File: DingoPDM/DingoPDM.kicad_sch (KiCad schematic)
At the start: 6 parts

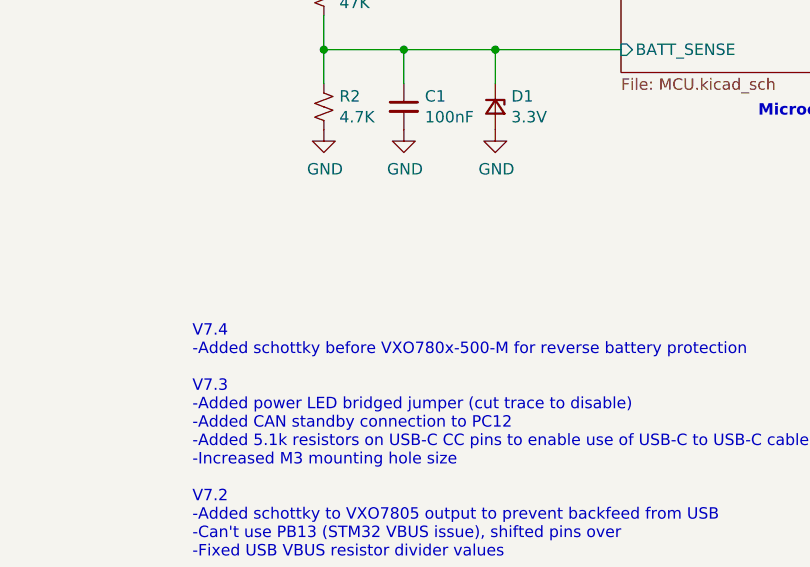
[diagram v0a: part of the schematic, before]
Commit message: add DC-DC converter options
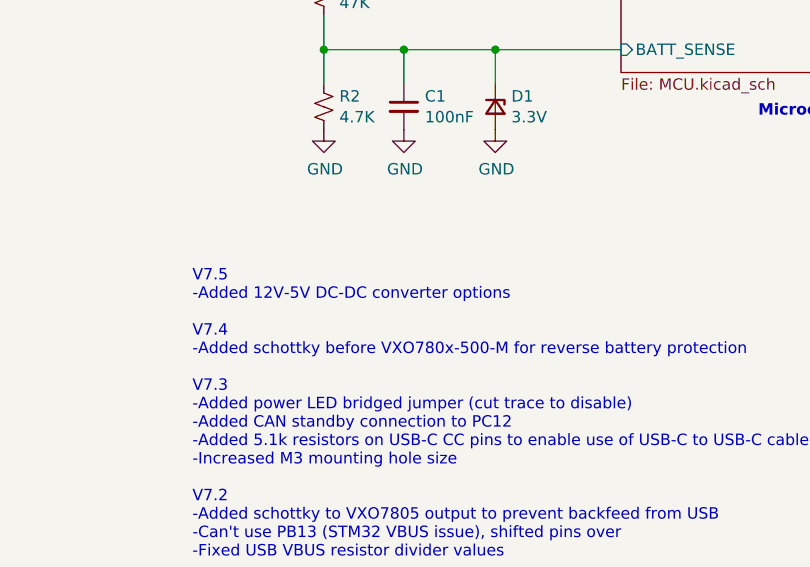
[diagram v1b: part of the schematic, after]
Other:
- note added: "V7.5 -Added 12V-5V DC-DC converter options V7.4 -Added schottky before VXO780x-500-M for reverse battery protection V7.3 -Added power LED bridged jumper (cut trace to disable) -Added CAN standby connection to PC12 -Added 5.1k resistors on USB-C CC pins to enable use of USB-C to USB-C cable -Increased M3 mounting hole size V7.2 -Added schottky to VXO7805 output to prevent backfeed from USB -Can't 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"
- note removed: "V7.4 -Added schottky before VXO780x-500-M for reverse battery protection V7.3 -Added power LED bridged jumper (cut trace to disable) -Added CAN standby connection to PC12 -Added 5.1k resistors on USB-C CC pins to enable use of USB-C to USB-C cable -Increased M3 mounting hole size V7.2 -Added schottky to VXO7805 output to prevent backfeed from USB -Can't use PB13 (STM32 VBUS issue), shifted pins o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"
- title: Dingo_PDM -> dingoPDM
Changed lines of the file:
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@@
 (kicad_sch
-	(version 20231120)
+	(version 20250114)
 	(generator "eeschema")
-	(generator_version "8.0")
+	(generator_version "9.0")
 	(paper "USLetter")
 	(title_block
-		(title "Dingo_PDM")
-		(date "2024-05-26")
-		(rev "v7.3")
+		(title "dingoPDM")
+		(date "2025-05-06")
+		(rev "v7.5")
 		(comment 3 "github.com/corygrant")
 		(comment 4 "Cory Grant")
+	)
+	(text "Microcontroller"
+		(exclude_from_sim no)
+		(at 132.715 120.65 0)
+		(effects
+			(font
+				(size 1.27 1.27)
+				(thickness 0.254)
+				(bold yes)
+			)
+			(justify left bottom)
+		)
+	)
+	(text "V7.5 \n-Added 12V-5V DC-DC converter options\n\nV7.4\n-Added schottky before VXO780x-500-M for reverse battery protection\n\nV7.3\n-Added power LED bridged jumper (cut trace to disable)\n-Added CAN standby connection to PC12\n-Added 5.1k resistors on USB-C CC pins to enable use of USB-C to USB-C cable\n-Increased M3 mounting hole size\n\nV7.2\n-Added schottky to VXO7805 output to prevent backfeed from USB\n-Can't use PB13 (STM32 VBUS issue), shifted pins over\n-Fixed USB VBUS resistor divider values\n\nV7.1\n-Fixed FRAM SCL/SDA backwards\n-Changed top copper fill from solid to thermal reliefs to make soldering easier\n-Added 2x status LEDs\n-Fixed silkscreen\n\nV7\n-Changed to STM32F446RET6\n-Added USB again, for DFU and easy settings change\n-Switched BTS724 to 2x BTS7008-2EPA\n-Added another op-amp for IS\n-Added boot selector again to enable DFU\n"
+		(exclude_from_sim no)
+		(at 69.85 196.215 0)
+		(effects
+			(font
+				(size 1.27 1.27)
+			)
+			(justify left bottom)
+		)
 	)
 	(junction
@@
 			(width 0)
 			(type default)
-		)
-	)
-	(text "Microcontroller"
-		(exclude_from_sim no)
-		(at 132.715 120.65 0)
-		(effects
-			(font
-				(size 1.27 1.27)
-				(thickness 0.254)
-				(bold yes)
-			)
-			(justify left bottom)
-		)
-	)
-	(text "V7.4\n-Added schottky before VXO780x-500-M for reverse battery protection\n\nV7.3\n-Added power LED bridged jumper (cut trace to disable)\n-Added CAN standby connection to PC12\n-Added 5.1k resistors on USB-C CC pins to enable use of USB-C to USB-C cable\n-Increased M3 mounting hole size\n\nV7.2\n-Added schottky to VXO7805 output to prevent backfeed from USB\n-Can't use PB13 (STM32 VBUS issue), shifted pins over\n-Fixed USB VBUS resistor divider values\n\nV7.1\n-Fixed FRAM SCL/SDA backwards\n-Changed top copper fill from solid to thermal reliefs to make soldering easier\n-Added 2x status LEDs\n-Fixed silkscreen\n\nV7\n-Changed to STM32F446RET6\n-Added USB again, for DFU and easy settings change\n-Switched BTS724 to 2x BTS7008-2EPA\n-Added another op-amp for IS\n-Added boot selector again to enable DFU\n"
-		(exclude_from_sim no)
-		(at 69.85 196.215 0)
-		(effects
-			(font
-				(size 1.27 1.27)
-			)
-			(justify left bottom)
 		)
 	)
@@
 		(at 117.475 63.5)
 		(size 43.18 52.07)
+		(exclude_from_sim no)
+		(in_bom yes)
+		(on_board yes)
+		(dnp no)
 		(fields_autoplaced yes)
 		(stroke
@@
 		(at 231.14 19.685)
 		(size 22.86 21.59)
+		(exclude_from_sim no)
+		(in_bom yes)
+		(on_board yes)
+		(dnp no)
 		(fields_autoplaced yes)
 		(stroke
@@
 		(at 231.14 51.435)
 		(size 22.86 21.59)
+		(exclude_from_sim no)
+		(in_bom yes)
+		(on_board yes)
+		(dnp no)
 		(fields_autoplaced yes)
 		(stroke
@@
 		(at 15.24 46.355)
 		(size 22.86 21.59)
+		(exclude_from_sim no)
+		(in_bom yes)
+		(on_board yes)
+		(dnp no)
 		(fields_autoplaced yes)
 		(stroke
@@
 		(at 14.605 116.84)
 		(size 22.86 21.59)
+		(exclude_from_sim no)
+		(in_bom yes)
+		(on_board yes)
+		(dnp no)
 		(fields_autoplaced yes)
 		(stroke
@@
 		(at 15.24 15.875)
 		(size 22.86 21.59)
+		(exclude_from_sim no)
+		(in_bom yes)
+		(on_board yes)
+		(dnp no)
 		(fields_autoplaced yes)
 		(stroke
@@
 		(at 14.605 144.145)
 		(size 22.86 21.59)
+		(exclude_from_sim no)
+		(in_bom yes)
+		(on_board yes)
+		(dnp no)
 		(fields_autoplaced yes)
 		(stroke
@@
 		)
 	)
+	(embedded_fonts no)
 )

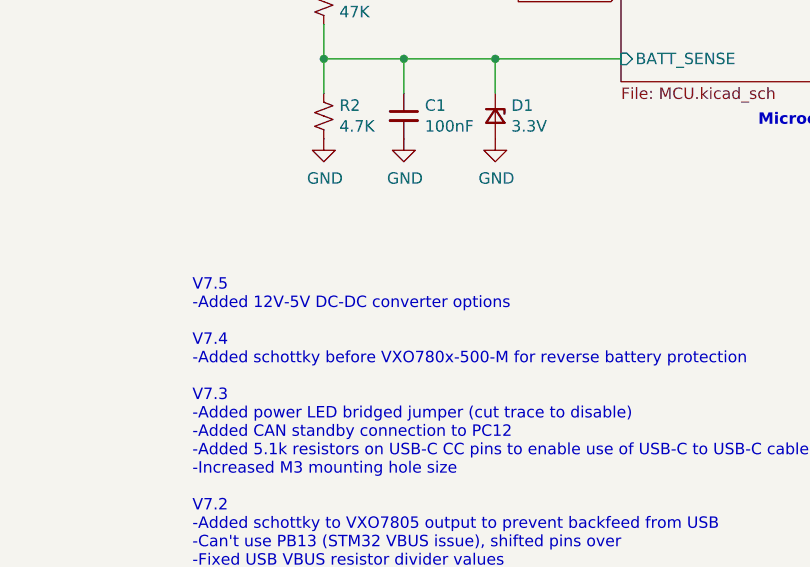
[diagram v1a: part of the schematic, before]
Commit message: add 5v cap
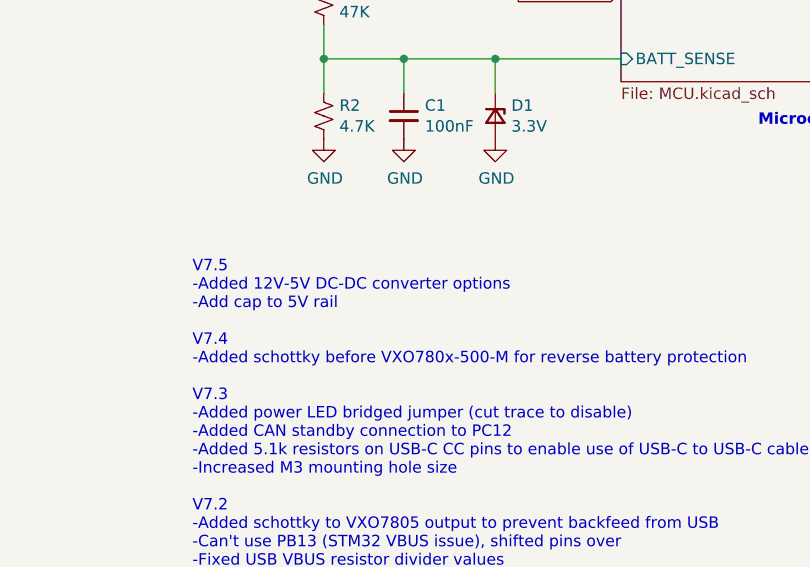
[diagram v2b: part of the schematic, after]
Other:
- note added: "V7.5 -Added 12V-5V DC-DC converter options -Add cap to 5V rail V7.4 -Added schottky before VXO780x-500-M for reverse battery protection V7.3 -Added power LED bridged jumper (cut trace to disable) -Added CAN standby connection to PC12 -Added 5.1k resistors on USB-C CC pins to enable use of USB-C to USB-C cable -Increased M3 mounting hole size V7.2 -Added schottky to VXO7805 output to prevent backf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"
- note removed: "V7.5 -Added 12V-5V DC-DC converter options V7.4 -Added schottky before VXO780x-500-M for reverse battery protection V7.3 -Added power LED bridged jumper (cut trace to disable) -Added CAN standby connection to PC12 -Added 5.1k resistors on USB-C CC pins to enable use of USB-C to USB-C cable -Increased M3 mounting hole size V7.2 -Added schottky to VXO7805 output to prevent backfeed from USB -Can't 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"
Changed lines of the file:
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@@
 	(title_block
 		(title "dingoPDM")
-		(date "2025-05-06")
+		(date "2025-06-16")
 		(rev "v7.5")
 		(comment 3 "github.com/corygrant")
@@
 		)
 	)
-	(text "V7.5 \n-Added 12V-5V DC-DC converter options\n\nV7.4\n-Added schottky before VXO780x-500-M for reverse battery protection\n\nV7.3\n-Added power LED bridged jumper (cut trace to disable)\n-Added CAN standby connection to PC12\n-Added 5.1k resistors on USB-C CC pins to enable use of USB-C to USB-C cable\n-Increased M3 mounting hole size\n\nV7.2\n-Added schottky to VXO7805 output to prevent backfeed from USB\n-Can't use PB13 (STM32 VBUS issue), shifted pins over\n-Fixed USB VBUS resistor divider values\n\nV7.1\n-Fixed FRAM SCL/SDA backwards\n-Changed top copper fill from solid to thermal reliefs to make soldering easier\n-Added 2x status LEDs\n-Fixed silkscreen\n\nV7\n-Changed to STM32F446RET6\n-Added USB again, for DFU and easy settings change\n-Switched BTS724 to 2x BTS7008-2EPA\n-Added another op-amp for IS\n-Added boot selector again to enable DFU\n"
+	(text "V7.5 \n-Added 12V-5V DC-DC converter options\n-Add cap to 5V rail\n\nV7.4\n-Added schottky before VXO780x-500-M for reverse battery protection\n\nV7.3\n-Added power LED bridged jumper (cut trace to disable)\n-Added CAN standby connection to PC12\n-Added 5.1k resistors on USB-C CC pins to enable use of USB-C to USB-C cable\n-Increased M3 mounting hole size\n\nV7.2\n-Added schottky to VXO7805 output to prevent backfeed from USB\n-Can't use PB13 (STM32 VBUS issue), shifted pins over\n-Fixed USB VBUS resistor divider values\n\nV7.1\n-Fixed FRAM SCL/SDA backwards\n-Changed top copper fill from solid to thermal reliefs to make soldering easier\n-Added 2x status LEDs\n-Fixed silkscreen\n\nV7\n-Changed to STM32F446RET6\n-Added USB again, for DFU and easy settings change\n-Switched BTS724 to 2x BTS7008-2EPA\n-Added another op-amp for IS\n-Added boot selector again to enable DFU\n"
 		(exclude_from_sim no)
 		(at 69.85 196.215 0)

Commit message: move footprints to project library
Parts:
- G1: footprint DRTLogo:DRTLogo -> dingoPDM:DRTLogo
- G2: footprint DRTLogo:DingoFaceNoFill -> dingoPDM:DingoFaceNoFill
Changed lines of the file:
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@@
 			)
 		)
-		(property "Footprint" "DRTLogo:DRTLogo"
+		(property "Footprint" "dingoPDM:DRTLogo"
 			(at 252.73 157.48 0)
 			(effects
@@
 			)
 		)
-		(property "Footprint" "DRTLogo:DingoFaceNoFill"
+		(property "Footprint" "dingoPDM:DingoFaceNoFill"
 			(at 252.73 164.465 0)
 			(effects

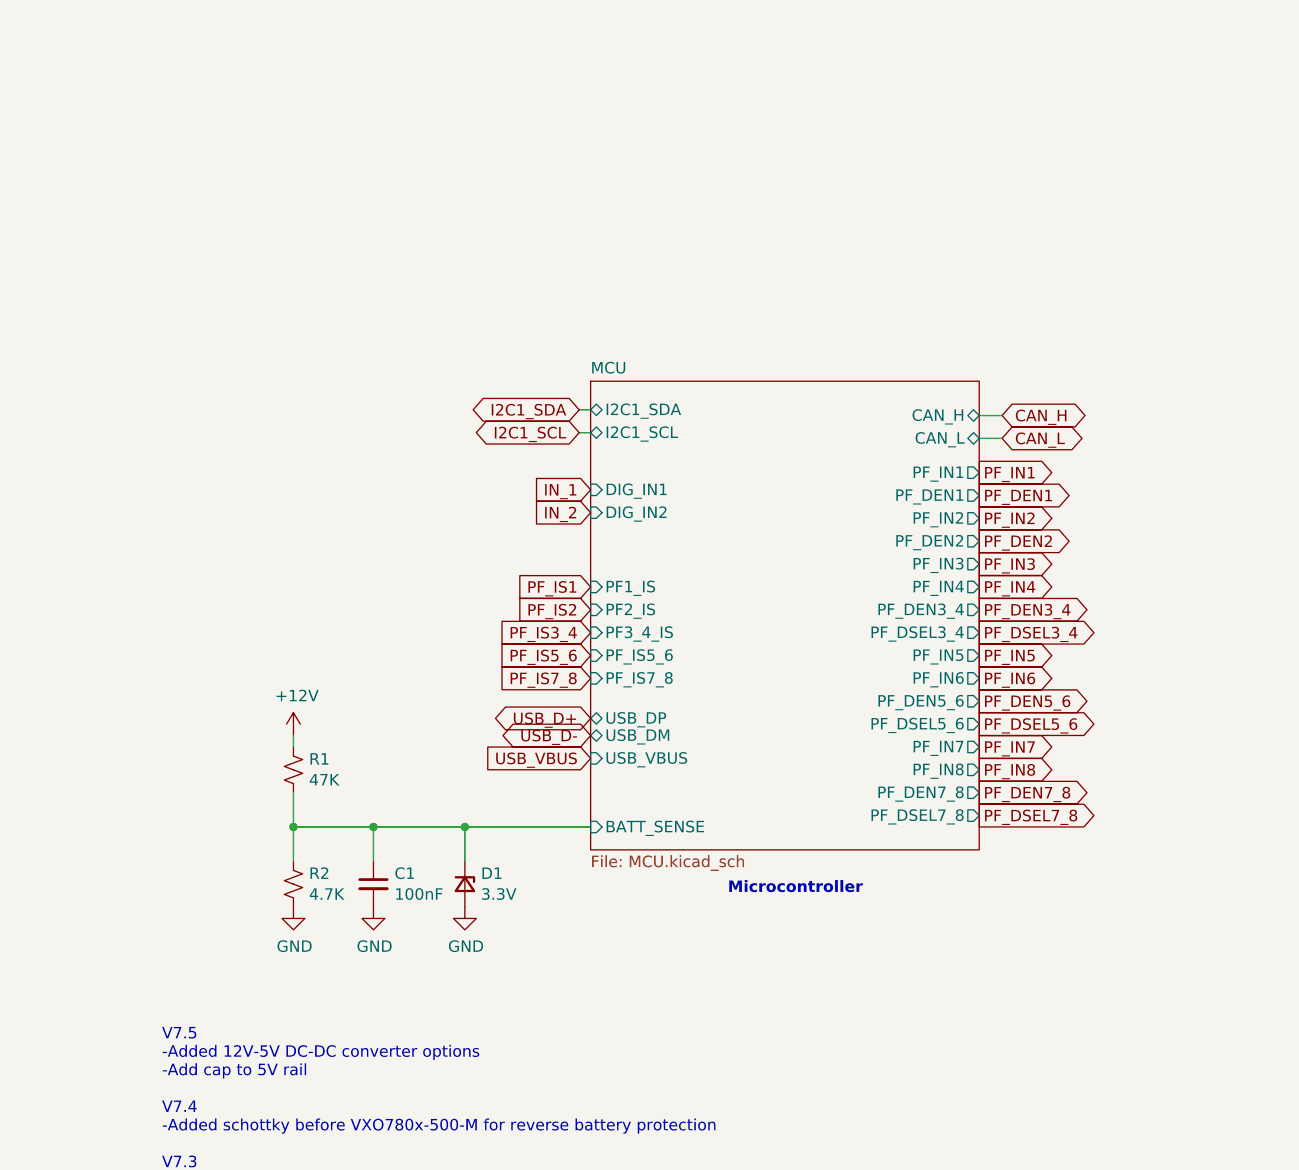
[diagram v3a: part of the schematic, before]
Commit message: make v7.6 changes, update can transceiver
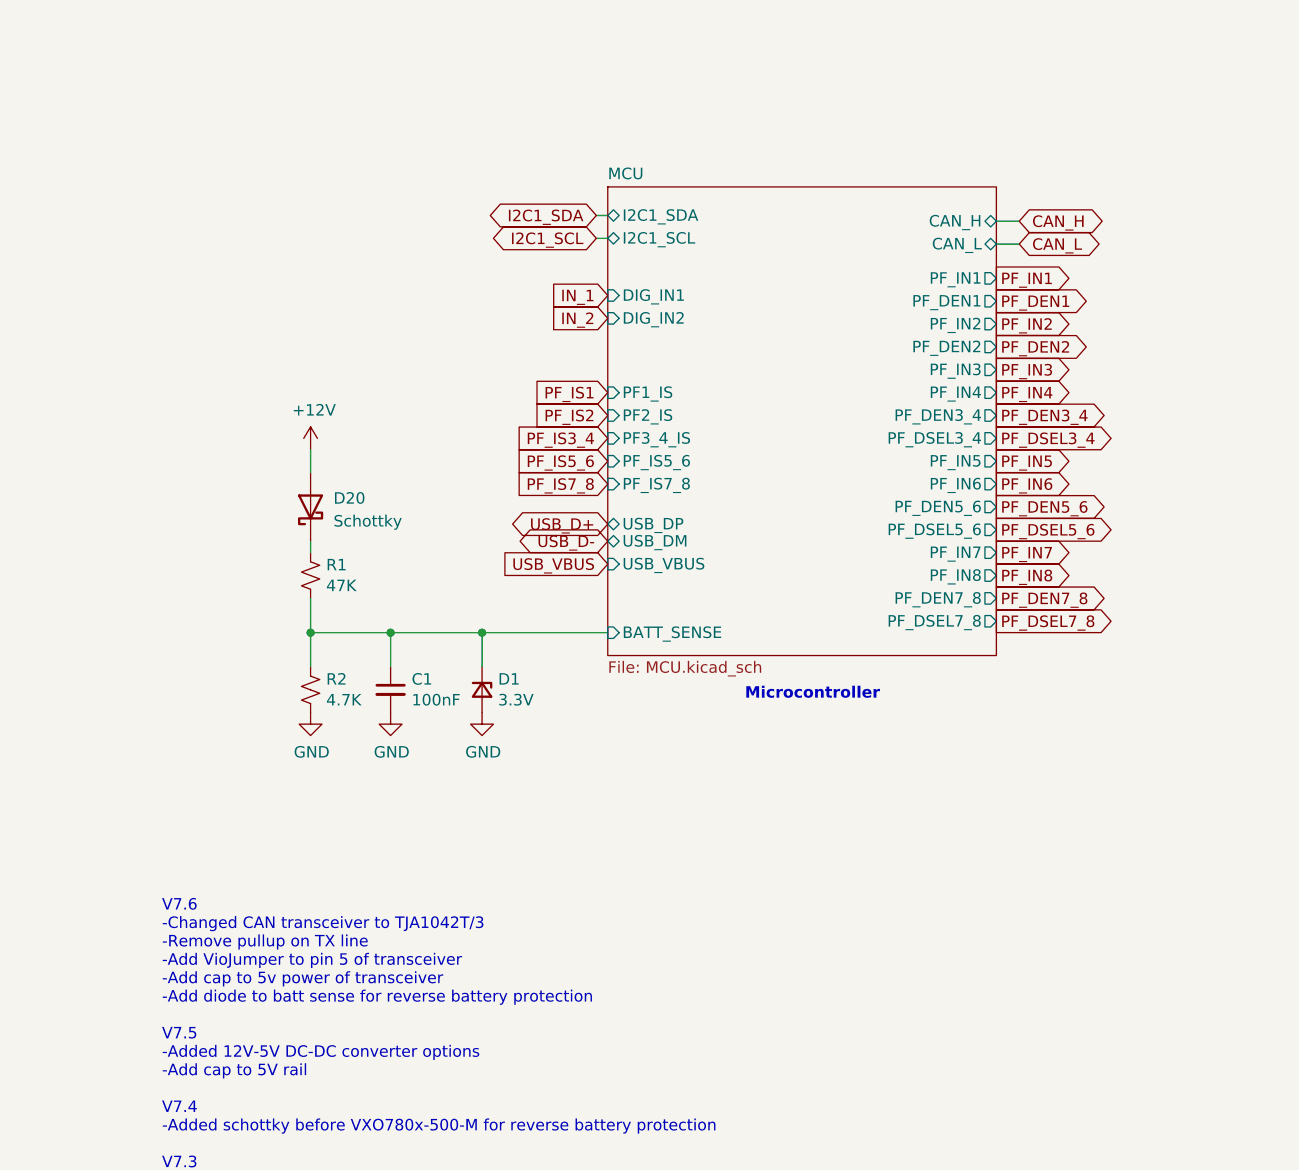
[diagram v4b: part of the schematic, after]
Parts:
- added D20: Schottky, Diode_SMD:D_SOD-123, symbol Device:D_Schottky
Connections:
- net +12V: now also D20.2 (A); no longer R1.1
- new net: D20.1 (K), R1.1
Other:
- note added: "V7.6 -Changed CAN transceiver to TJA1042T/3 -Remove pullup on TX line -Add VioJumper to pin 5 of transceiver -Add cap to 5v power of transceiver -Add diode to batt sense for reverse battery protection V7.5 -Added 12V-5V DC-DC converter options -Add cap to 5V rail V7.4 -Added schottky before VXO780x-500-M for reverse battery protection V7.3 -Added power LED bridged jumper (cut trace to disable) -A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"
- note removed: "V7.5 -Added 12V-5V DC-DC converter options -Add cap to 5V rail V7.4 -Added schottky before VXO780x-500-M for reverse battery protection V7.3 -Added power LED bridged jumper (cut trace to disable) -Added CAN standby connection to PC12 -Added 5.1k resistors on USB-C CC pins to enable use of USB-C to USB-C cable -Increased M3 mounting hole size V7.2 -Added schottky to VXO7805 output to prevent backf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"
- moved on the sheet: C1, D1, R1, R2
